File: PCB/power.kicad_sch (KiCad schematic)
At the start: 21 parts, among them U6 TLV62569DBVR, U7 TLV62569DBVR, U8 TLV62569DBVR

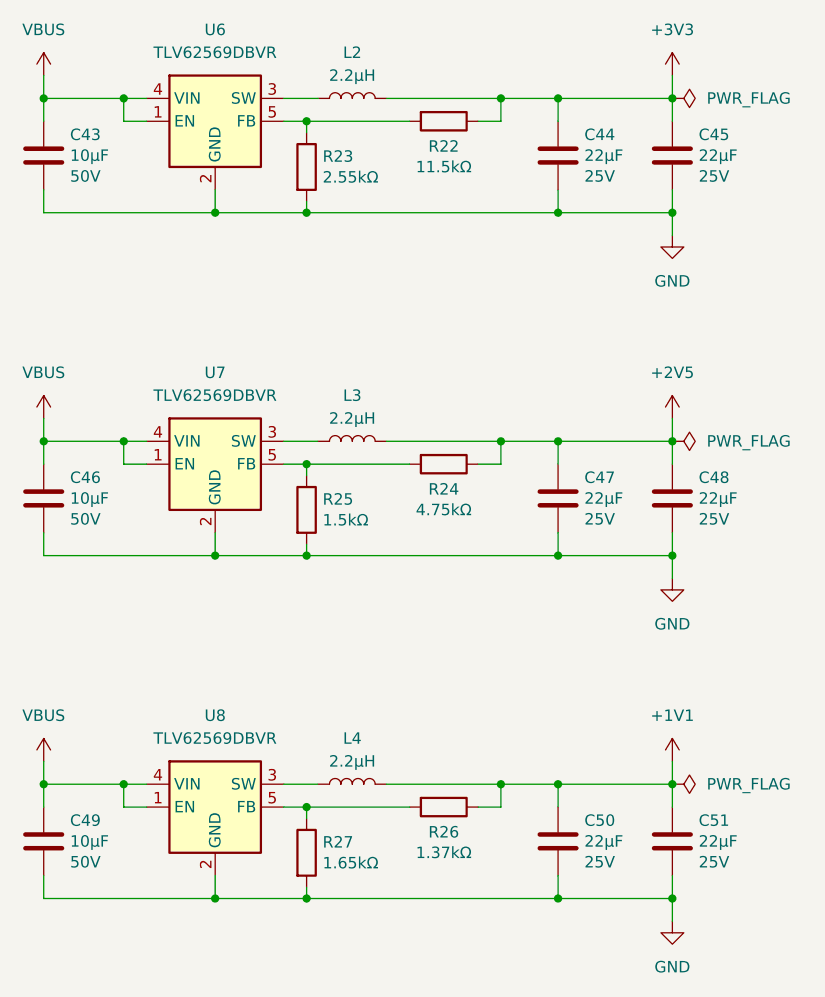
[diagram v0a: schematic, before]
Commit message: Fan-out the FPGA
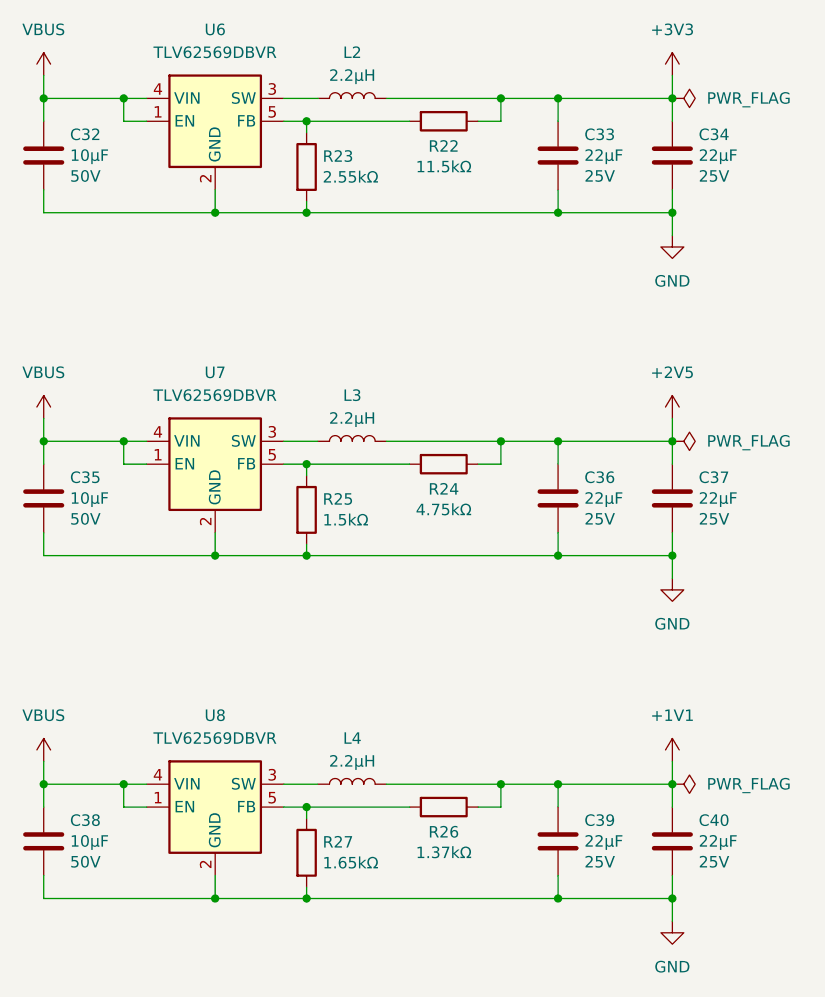
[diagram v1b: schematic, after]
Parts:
- renumbered C43 to C32, C44 to C33, C45 to C34, C46 to C35, C47 to C36, C48 to C37, C49 to C38, C50 to C39, C51 to C40
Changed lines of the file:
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@@
 		(dnp no)
 		(fields_autoplaced yes)
-		(property "Reference" "#PWR074"
+		(property "Reference" "#PWR067"
 			(at 171.45 110.49 0)
 			(effects
@@
 			(project "clavier"
 				(path "/6362c6e0-59ef-40d3-b6e0-7e9dfe7b9b20/0c8a9398-ddd2-4230-9850-fe0f46e922ad"
-					(reference "#PWR074")
+					(reference "#PWR067")
 					(unit 1)
 				)
@@
 		(dnp no)
 		(fields_autoplaced yes)
-		(property "Reference" "#PWR071"
+		(property "Reference" "#PWR064"
 			(at 171.45 72.39 0)
 			(effects
@@
 			(project "clavier"
 				(path "/6362c6e0-59ef-40d3-b6e0-7e9dfe7b9b20/0c8a9398-ddd2-4230-9850-fe0f46e922ad"
-					(reference "#PWR071")
+					(reference "#PWR064")
 					(unit 1)
 				)
@@
 		(on_board yes)
 		(dnp no)
-		(property "Reference" "C45"
+		(property "Reference" "C34"
 			(at 174.371 54.8386 0)
 			(effects
@@
 			(project "clavier"
 				(path "/6362c6e0-59ef-40d3-b6e0-7e9dfe7b9b20/0c8a9398-ddd2-4230-9850-fe0f46e922ad"
-					(reference "C45")
+					(reference "C34")
 					(unit 1)
 				)
@@
 		(on_board yes)
 		(dnp no)
-		(property "Reference" "C47"
+		(property "Reference" "C36"
 			(at 161.671 92.9386 0)
 			(effects
@@
 			(project "clavier"
 				(path "/6362c6e0-59ef-40d3-b6e0-7e9dfe7b9b20/0c8a9398-ddd2-4230-9850-fe0f46e922ad"
-					(reference "C47")
+					(reference "C36")
 					(unit 1)
 				)
@@
 		(dnp no)
 		(fields_autoplaced yes)
-		(property "Reference" "#PWR075"
+		(property "Reference" "#PWR068"
 			(at 101.6 128.27 0)
 			(effects
@@
 			(project "clavier"
 				(path "/6362c6e0-59ef-40d3-b6e0-7e9dfe7b9b20/0c8a9398-ddd2-4230-9850-fe0f46e922ad"
-					(reference "#PWR075")
+					(reference "#PWR068")
 					(unit 1)
 				)
@@
 		(on_board yes)
 		(dnp no)
-		(property "Reference" "C43"
+		(property "Reference" "C32"
 			(at 104.521 54.8386 0)
 			(effects
@@
 			(project "clavier"
 				(path "/6362c6e0-59ef-40d3-b6e0-7e9dfe7b9b20/0c8a9398-ddd2-4230-9850-fe0f46e922ad"
-					(reference "C43")
+					(reference "C32")
 					(unit 1)
 				)
@@
 		(dnp no)
 		(fields_autoplaced yes)
-		(property "Reference" "#PWR077"
+		(property "Reference" "#PWR070"
 			(at 171.45 148.59 0)
 			(effects
@@
 			(project "clavier"
 				(path "/6362c6e0-59ef-40d3-b6e0-7e9dfe7b9b20/0c8a9398-ddd2-4230-9850-fe0f46e922ad"
-					(reference "#PWR077")
+					(reference "#PWR070")
 					(unit 1)
 				)
@@
 		(dnp no)
 		(fields_autoplaced yes)
-		(property "Reference" "#PWR069"
+		(property "Reference" "#PWR062"
 			(at 101.6 52.07 0)
 			(effects
@@
 			(project ""
 				(path "/6362c6e0-59ef-40d3-b6e0-7e9dfe7b9b20/0c8a9398-ddd2-4230-9850-fe0f46e922ad"
-					(reference "#PWR069")
+					(reference "#PWR062")
 					(unit 1)
 				)
@@
 		(dnp no)
 		(fields_autoplaced yes)
-		(property "Reference" "#PWR072"
+		(property "Reference" "#PWR065"
 			(at 101.6 90.17 0)
 			(effects
@@
 			(project "clavier"
 				(path "/6362c6e0-59ef-40d3-b6e0-7e9dfe7b9b20/0c8a9398-ddd2-4230-9850-fe0f46e922ad"
-					(reference "#PWR072")
+					(reference "#PWR065")
 					(unit 1)
 				)
@@
 		(on_board yes)
 		(dnp no)
-		(property "Reference" "C51"
+		(property "Reference" "C40"
 			(at 174.371 131.0386 0)
 			(effects
@@
 			(project "clavier"
 				(path "/6362c6e0-59ef-40d3-b6e0-7e9dfe7b9b20/0c8a9398-ddd2-4230-9850-fe0f46e922ad"
-					(reference "C51")
+					(reference "C40")
 					(unit 1)
 				)
@@
 		(dnp no)
 		(fields_autoplaced yes)
-		(property "Reference" "#PWR070"
+		(property "Reference" "#PWR063"
 			(at 171.45 52.07 0)
 			(effects
@@
 			(project "clavier"
 				(path "/6362c6e0-59ef-40d3-b6e0-7e9dfe7b9b20/0c8a9398-ddd2-4230-9850-fe0f46e922ad"
-					(reference "#PWR070")
+					(reference "#PWR063")
 					(unit 1)
 				)
@@
 		(on_board yes)
 		(dnp no)
-		(property "Reference" "C50"
+		(property "Reference" "C39"
 			(at 161.671 131.0386 0)
 			(effects
@@
 			(project "clavier"
 				(path "/6362c6e0-59ef-40d3-b6e0-7e9dfe7b9b20/0c8a9398-ddd2-4230-9850-fe0f46e922ad"
-					(reference "C50")
+					(reference "C39")
 					(unit 1)
 				)
@@
 		(dnp no)
 		(fields_autoplaced yes)
-		(property "Reference" "#PWR076"
+		(property "Reference" "#PWR069"
 			(at 171.45 128.27 0)
 			(effects
@@
 			(project "clavier"
 				(path "/6362c6e0-59ef-40d3-b6e0-7e9dfe7b9b20/0c8a9398-ddd2-4230-9850-fe0f46e922ad"
-					(reference "#PWR076")
+					(reference "#PWR069")
 					(unit 1)
 				)
@@
 		(on_board yes)
 		(dnp no)
-		(property "Reference" "C44"
+		(property "Reference" "C33"
 			(at 161.671 54.8386 0)
 			(effects
@@
 			(project "clavier"
 				(path "/6362c6e0-59ef-40d3-b6e0-7e9dfe7b9b20/0c8a9398-ddd2-4230-9850-fe0f46e922ad"
-					(reference "C44")
+					(reference "C33")
 					(unit 1)
 				)
@@
 		(on_board yes)
 		(dnp no)
-		(property "Reference" "C49"
+		(property "Reference" "C38"
 			(at 104.521 131.0386 0)
 			(effects
@@
 			(project "clavier"
 				(path "/6362c6e0-59ef-40d3-b6e0-7e9dfe7b9b20/0c8a9398-ddd2-4230-9850-fe0f46e922ad"
-					(reference "C49")
+					(reference "C38")
 					(unit 1)
 				)
@@
 		(on_board yes)
 		(dnp no)
-		(property "Reference" "C46"
+		(property "Reference" "C35"
 			(at 104.521 92.9386 0)
 			(effects
@@
 			(project "clavier"
 				(path "/6362c6e0-59ef-40d3-b6e0-7e9dfe7b9b20/0c8a9398-ddd2-4230-9850-fe0f46e922ad"
-					(reference "C46")
+					(reference "C35")
 					(unit 1)
 				)
@@
 		(dnp no)
 		(fields_autoplaced yes)
-		(property "Reference" "#PWR073"
+		(property "Reference" "#PWR066"
 			(at 171.45 90.17 0)
 			(effects
@@
 			(project "clavier"
 				(path "/6362c6e0-59ef-40d3-b6e0-7e9dfe7b9b20/0c8a9398-ddd2-4230-9850-fe0f46e922ad"
-					(reference "#PWR073")
+					(reference "#PWR066")
 					(unit 1)
 				)
@@
 		(on_board yes)
 		(dnp no)
-		(property "Reference" "C48"
+		(property "Reference" "C37"
 			(at 174.371 92.9386 0)
 			(effects
@@
 			(project "clavier"
 				(path "/6362c6e0-59ef-40d3-b6e0-7e9dfe7b9b20/0c8a9398-ddd2-4230-9850-fe0f46e922ad"
-					(reference "C48")
-					(unit 1)
-				)
+					(reference "C37")
+					(unit 1)
+				)

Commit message: Add ESD protection
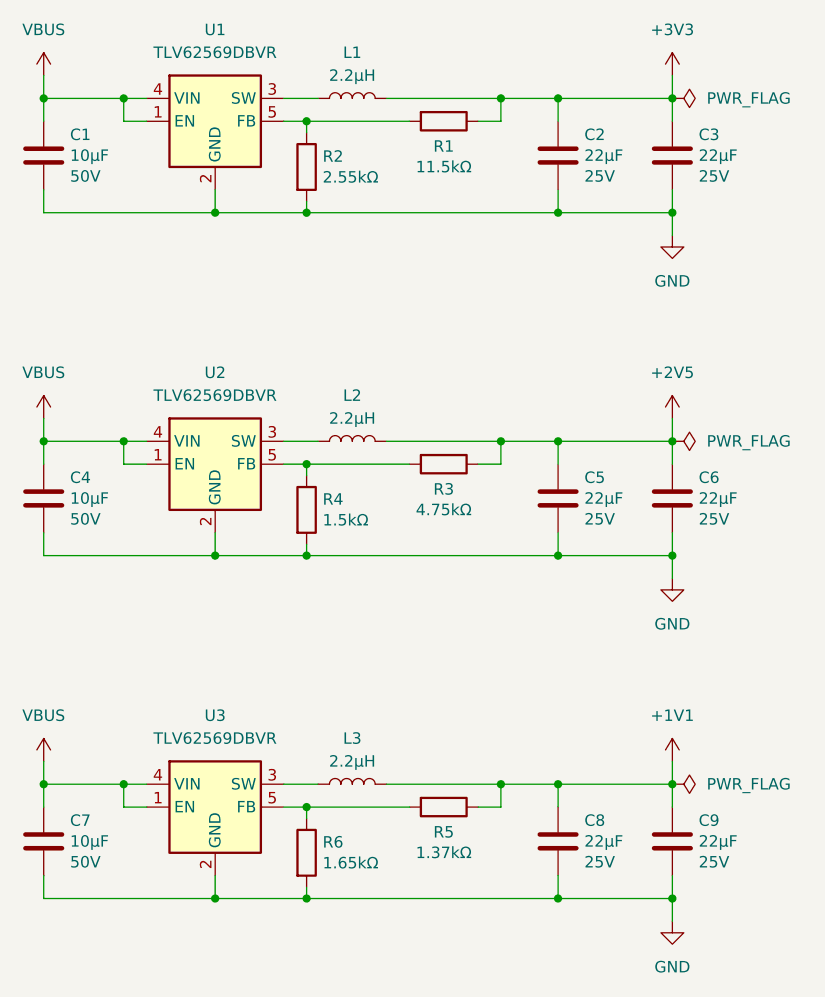
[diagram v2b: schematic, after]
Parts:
- renumbered C32 to C1, C33 to C2, C34 to C3, C35 to C4, C36 to C5, C37 to C6, C38 to C7, C39 to C8, C40 to C9, L2 to L1, L3 to L2, L4 to L3, R22 to R1, R23 to R2, R24 to R3, R25 to R4, R26 to R5, R27 to R6, U6 to U1, U7 to U2, U8 to U3

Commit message: Complete the PCB routing
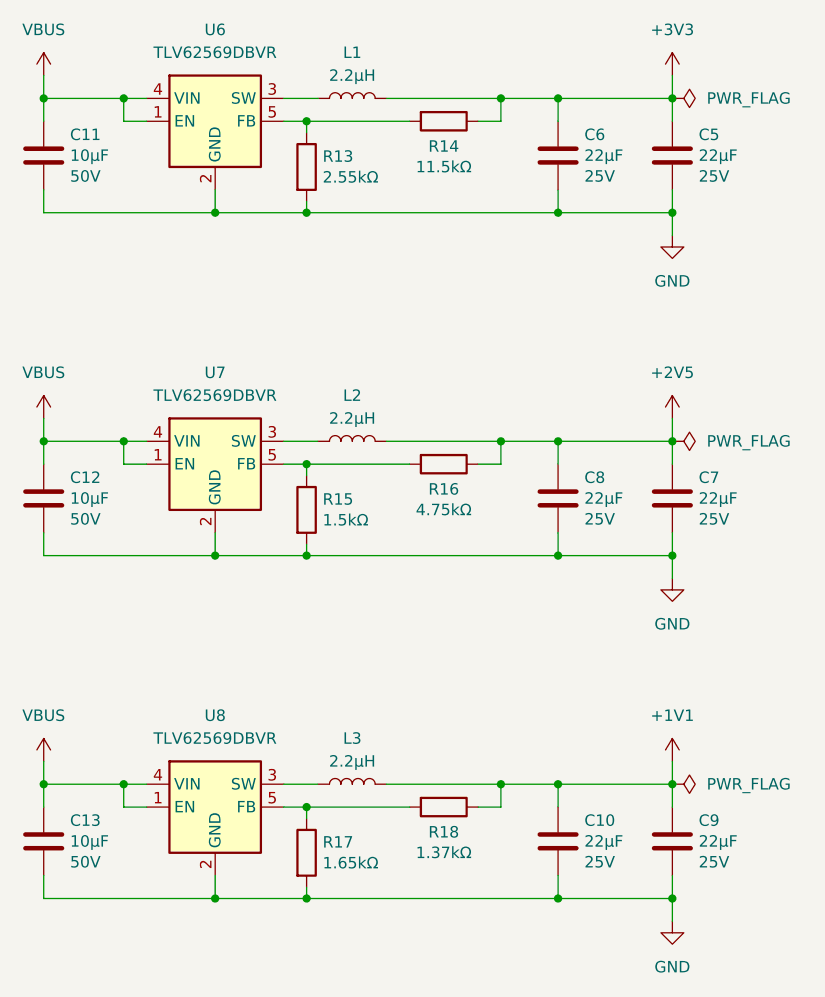
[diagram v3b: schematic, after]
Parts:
- renumbered C8 to C10, C1 to C11, C4 to C12, C7 to C13, C3 to C5, C2 to C6, C6 to C7, C5 to C8, R2 to R13, R1 to R14, R4 to R15, R3 to R16, R6 to R17, R5 to R18, U1 to U6, U2 to U7, U3 to U8
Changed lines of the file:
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@@
 	(title_block
 		(title "Clavier - Power supplies")
-		(date "2025-06-21")
+		(date "2025-06-22")
 		(rev "1.0")
 		(company "Copyright (c) 2025 L. Sartory")
@@
 		(dnp no)
 		(fields_autoplaced yes)
-		(property "Reference" "U1"
+		(property "Reference" "U6"
 			(at 120.65 43.18 0)
 			(effects
@@
 			(project ""
 				(path "/6362c6e0-59ef-40d3-b6e0-7e9dfe7b9b20/0c8a9398-ddd2-4230-9850-fe0f46e922ad"
-					(reference "U1")
+					(reference "U6")
 					(unit 1)
 				)
@@
 		(on_board yes)
 		(dnp no)
-		(property "Reference" "R1"
+		(property "Reference" "R14"
 			(at 146.05 56.134 90)
 			(effects
@@
 			(project "clavier"
 				(path "/6362c6e0-59ef-40d3-b6e0-7e9dfe7b9b20/0c8a9398-ddd2-4230-9850-fe0f46e922ad"
-					(reference "R1")
+					(reference "R14")
 					(unit 1)
 				)
@@
 		(dnp no)
 		(fields_autoplaced yes)
-		(property "Reference" "U2"
+		(property "Reference" "U7"
 			(at 120.65 81.28 0)
 			(effects
@@
 			(project "clavier"
 				(path "/6362c6e0-59ef-40d3-b6e0-7e9dfe7b9b20/0c8a9398-ddd2-4230-9850-fe0f46e922ad"
-					(reference "U2")
+					(reference "U7")
 					(unit 1)
 				)
@@
 		(on_board yes)
 		(dnp no)
-		(property "Reference" "C3"
+		(property "Reference" "C5"
 			(at 174.371 54.8386 0)
 			(effects
@@
 			(project "clavier"
 				(path "/6362c6e0-59ef-40d3-b6e0-7e9dfe7b9b20/0c8a9398-ddd2-4230-9850-fe0f46e922ad"
-					(reference "C3")
+					(reference "C5")
 					(unit 1)
 				)
@@
 		(dnp no)
 		(fields_autoplaced yes)
-		(property "Reference" "U3"
+		(property "Reference" "U8"
 			(at 120.65 119.38 0)
 			(effects
@@
 			(project "clavier"
 				(path "/6362c6e0-59ef-40d3-b6e0-7e9dfe7b9b20/0c8a9398-ddd2-4230-9850-fe0f46e922ad"
-					(reference "U3")
+					(reference "U8")
 					(unit 1)
 				)
@@
 		(on_board yes)
 		(dnp no)
-		(property "Reference" "C5"
+		(property "Reference" "C8"
 			(at 161.671 92.9386 0)
 			(effects
@@
 			(project "clavier"
 				(path "/6362c6e0-59ef-40d3-b6e0-7e9dfe7b9b20/0c8a9398-ddd2-4230-9850-fe0f46e922ad"
-					(reference "C5")
+					(reference "C8")
 					(unit 1)
 				)
@@
 		(on_board yes)
 		(dnp no)
-		(property "Reference" "C1"
+		(property "Reference" "C11"
 			(at 104.521 54.8386 0)
 			(effects
@@
 			(project "clavier"
 				(path "/6362c6e0-59ef-40d3-b6e0-7e9dfe7b9b20/0c8a9398-ddd2-4230-9850-fe0f46e922ad"
-					(reference "C1")
+					(reference "C11")
 					(unit 1)
 				)
@@
 		(on_board yes)
 		(dnp no)
-		(property "Reference" "R3"
+		(property "Reference" "R16"
 			(at 146.05 94.234 90)
 			(effects
@@
 			(project "clavier"
 				(path "/6362c6e0-59ef-40d3-b6e0-7e9dfe7b9b20/0c8a9398-ddd2-4230-9850-fe0f46e922ad"
-					(reference "R3")
+					(reference "R16")
 					(unit 1)
 				)
@@
 		(on_board yes)
 		(dnp no)
-		(property "Reference" "R5"
+		(property "Reference" "R18"
 			(at 146.05 132.334 90)
 			(effects
@@
 			(project "clavier"
 				(path "/6362c6e0-59ef-40d3-b6e0-7e9dfe7b9b20/0c8a9398-ddd2-4230-9850-fe0f46e922ad"
-					(reference "R5")
+					(reference "R18")
 					(unit 1)
 				)
@@
 		(on_board yes)
 		(dnp no)
-		(property "Reference" "R4"
+		(property "Reference" "R15"
 			(at 132.588 95.3516 0)
 			(effects
@@
 			(project "clavier"
 				(path "/6362c6e0-59ef-40d3-b6e0-7e9dfe7b9b20/0c8a9398-ddd2-4230-9850-fe0f46e922ad"
-					(reference "R4")
+					(reference "R15")
 					(unit 1)
 				)
@@
 		(on_board yes)
 		(dnp no)
-		(property "Reference" "C8"
+		(property "Reference" "C10"
 			(at 161.671 131.0386 0)
 			(effects
@@
 			(project "clavier"
 				(path "/6362c6e0-59ef-40d3-b6e0-7e9dfe7b9b20/0c8a9398-ddd2-4230-9850-fe0f46e922ad"
-					(reference "C8")
+					(reference "C10")
 					(unit 1)
 				)
@@
 		(on_board yes)
 		(dnp no)
-		(property "Reference" "C2"
+		(property "Reference" "C6"
 			(at 161.671 54.8386 0)
 			(effects
@@
 			(project "clavier"
 				(path "/6362c6e0-59ef-40d3-b6e0-7e9dfe7b9b20/0c8a9398-ddd2-4230-9850-fe0f46e922ad"
-					(reference "C2")
+					(reference "C6")
 					(unit 1)
 				)
@@
 		(on_board yes)
 		(dnp no)
-		(property "Reference" "R6"
+		(property "Reference" "R17"
 			(at 132.588 133.4516 0)
 			(effects
@@
 			(project "clavier"
 				(path "/6362c6e0-59ef-40d3-b6e0-7e9dfe7b9b20/0c8a9398-ddd2-4230-9850-fe0f46e922ad"
-					(reference "R6")
+					(reference "R17")
 					(unit 1)
 				)
@@
 		(on_board yes)
 		(dnp no)
-		(property "Reference" "R2"
+		(property "Reference" "R13"
 			(at 132.588 57.2516 0)
 			(effects
@@
 			(project "clavier"
 				(path "/6362c6e0-59ef-40d3-b6e0-7e9dfe7b9b20/0c8a9398-ddd2-4230-9850-fe0f46e922ad"
-					(reference "R2")
+					(reference "R13")
 					(unit 1)
 				)
@@
 		(on_board yes)
 		(dnp no)
-		(property "Reference" "C7"
+		(property "Reference" "C13"
 			(at 104.521 131.0386 0)
 			(effects
@@
 			(project "clavier"
 				(path "/6362c6e0-59ef-40d3-b6e0-7e9dfe7b9b20/0c8a9398-ddd2-4230-9850-fe0f46e922ad"
-					(reference "C7")
+					(reference "C13")
 					(unit 1)
 				)
@@
 		(on_board yes)
 		(dnp no)
-		(property "Reference" "C4"
+		(property "Reference" "C12"
 			(at 104.521 92.9386 0)
 			(effects
@@
 			(project "clavier"
 				(path "/6362c6e0-59ef-40d3-b6e0-7e9dfe7b9b20/0c8a9398-ddd2-4230-9850-fe0f46e922ad"
-					(reference "C4")
+					(reference "C12")
 					(unit 1)
 				)
@@
 		(on_board yes)
 		(dnp no)
-		(property "Reference" "C6"
+		(property "Reference" "C7"
 			(at 174.371 92.9386 0)
 			(effects
@@
 			(project "clavier"
 				(path "/6362c6e0-59ef-40d3-b6e0-7e9dfe7b9b20/0c8a9398-ddd2-4230-9850-fe0f46e922ad"
-					(reference "C6")
+					(reference "C7")
 					(unit 1)
 				)
